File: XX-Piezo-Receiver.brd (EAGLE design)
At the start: 30.7 x 26.2 mm, 10 parts, among them IC1 TL072D, IC2 L78LXXBD/CD, J1 AVR_SPI_PROG_3X2PTH, U1 ATMEGA1284P-AU

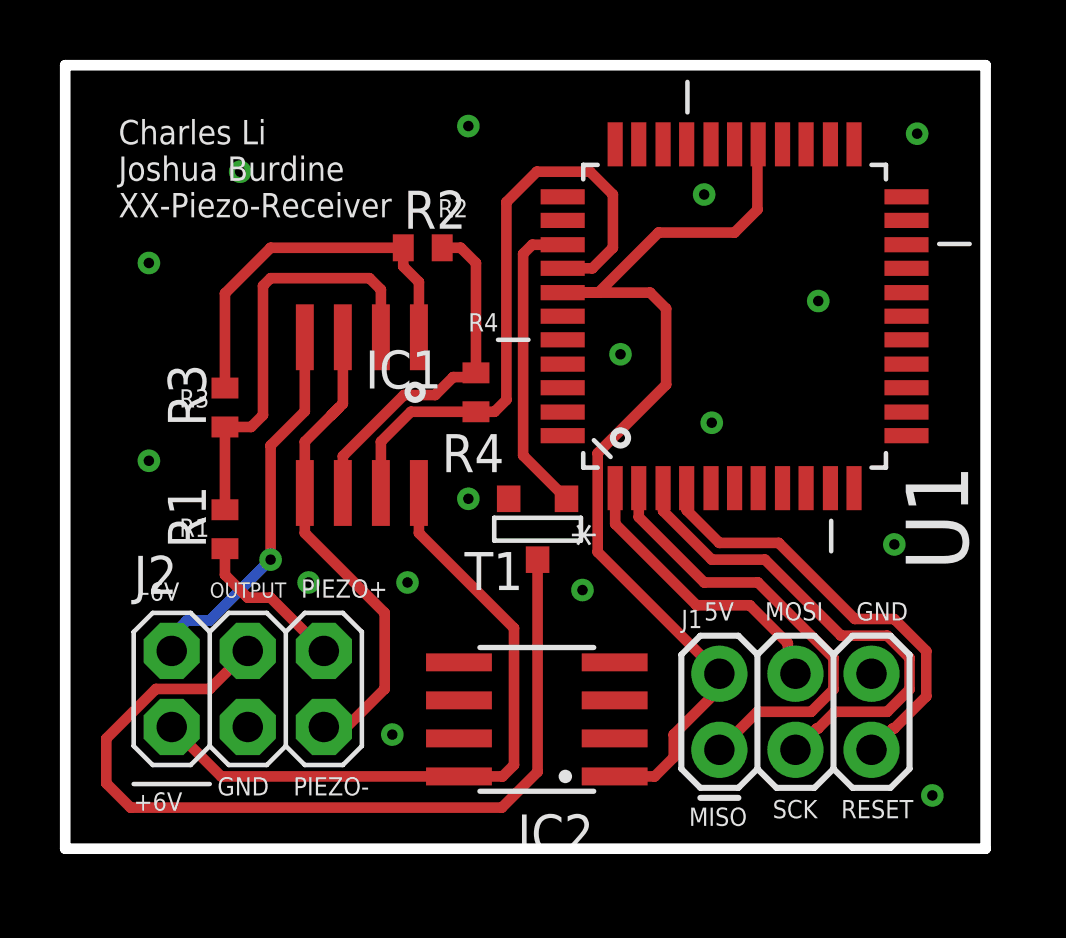
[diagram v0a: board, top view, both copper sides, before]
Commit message: Added decoupling caps and mount hole.
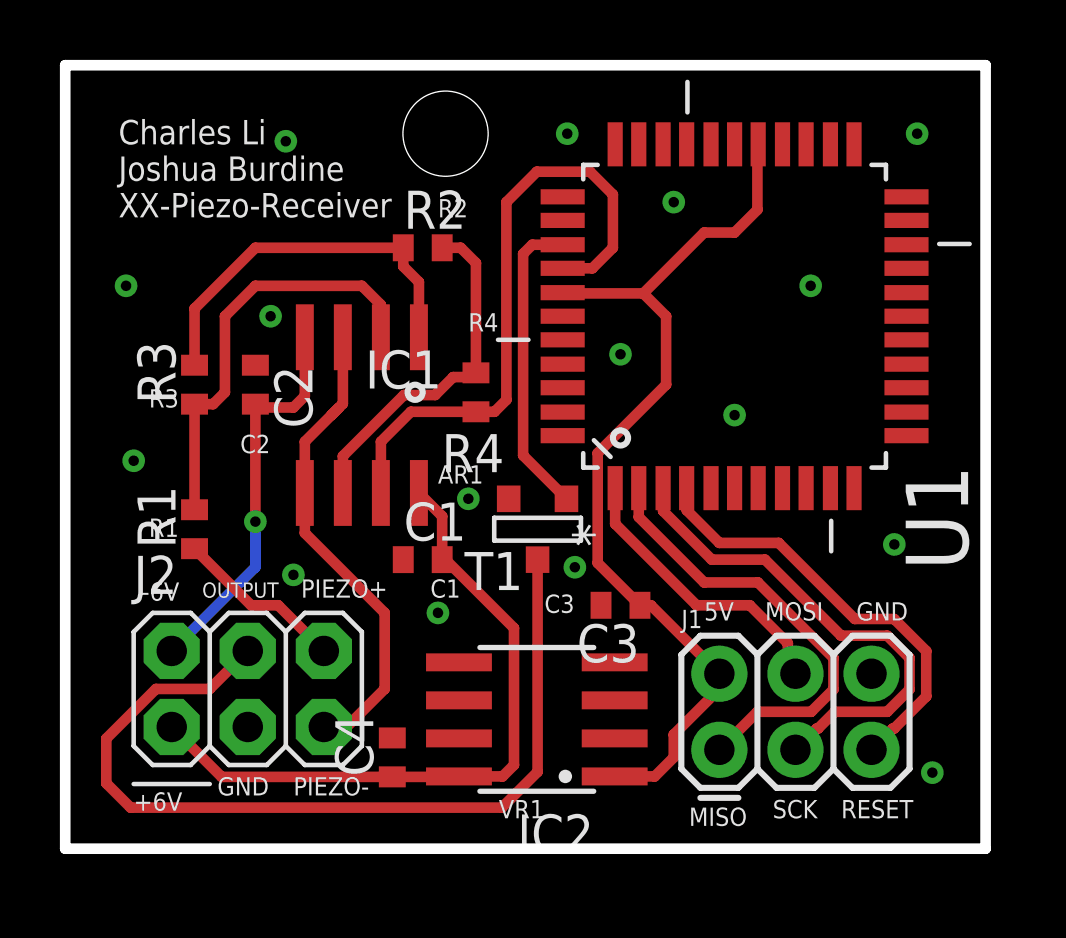
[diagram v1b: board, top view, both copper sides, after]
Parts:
- added C1, C2, C3: 0.1uF, rcl:C0402
- added C4: 0.33uF, rcl:C0402
- moved R3 1.27 mm to (4.32, 15.5)
- moved R1 1.02 mm to (4.32, 10.7)
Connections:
- net +5V: now also C3.1
- net +6V: now also C1.2, C4.1
- net -6V: now also C2.2
- net GND: now also C1.1, C2.1, C3.2, C4.2, IC2.3, IC2.6, IC2.7
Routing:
- net +5V: track 35.1 -> 31.4 mm
- net PIEZO+: track 5.23 -> 5.73 mm
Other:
- board text added: "AR1"
- board text added: "C1"
- board text added: "C2"
- board text added: "C3"
- board text added: "VR1"

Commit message: Change to 0603 components. Add new lin reg. Add new mount hole.
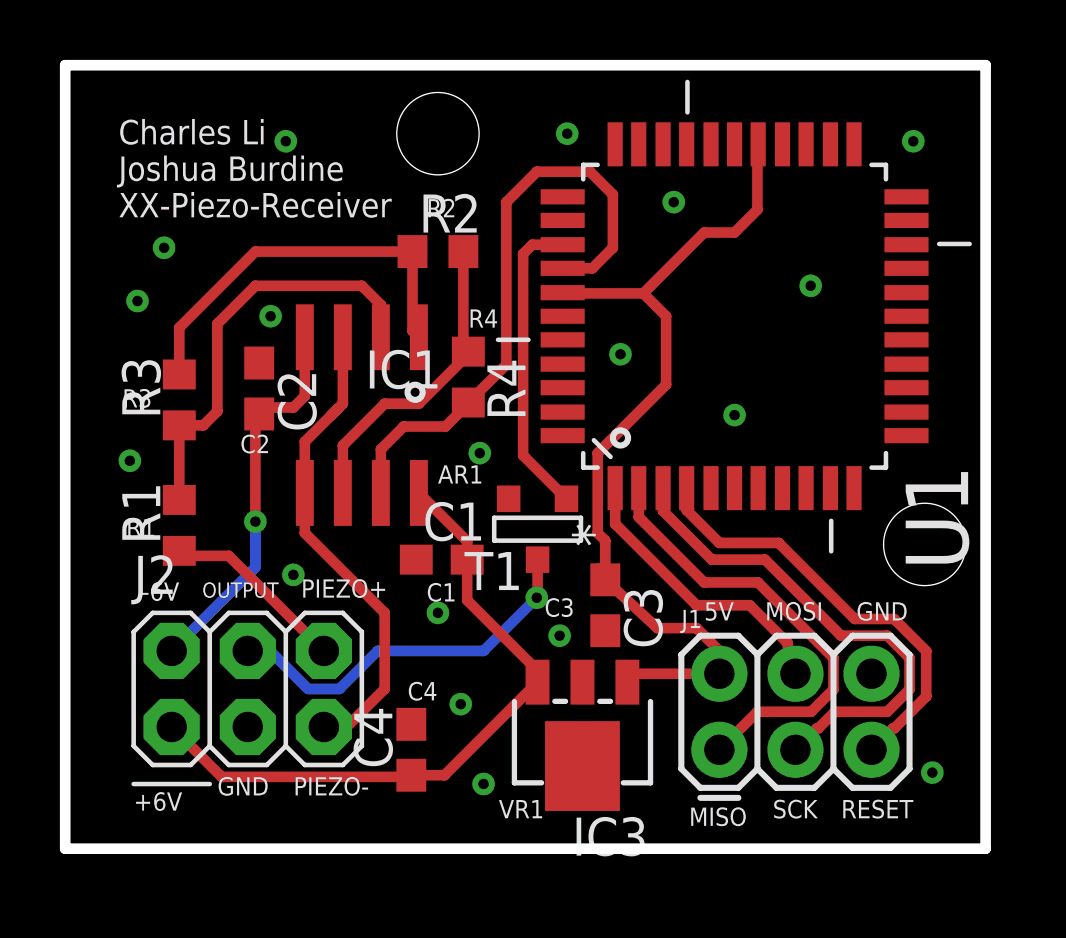
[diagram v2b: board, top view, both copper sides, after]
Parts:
- removed IC2: L78LXXBD/CD, v-reg-3:SO08
- added IC3: L78LXXCU/BU, v-reg-3:SOT89
- C1, C2, C3, C4: device rcl:C0402 -> rcl:C0603
- R1, R2, R3, R4: device rcl:R0402 -> rcl:R0603
- moved R3 0.72 mm to (3.81, 15.0)
- moved C4 0.68 mm to (11.6, 3.30)
- moved C1 0.63 mm to (12.6, 9.65)
- moved R4 0.57 mm to (13.5, 15.7)
- moved R1 0.52 mm to (3.81, 10.8)
- moved R2 0.52 mm to (12.4, 19.9)
- moved C3 0.51 mm to (18.0, 8.13), turned to 270 degrees
- moved C2 0.18 mm to (6.48, 15.4)
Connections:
- net +5V: now also IC3.1; no longer IC2.1
- net +6V: now also IC3.3; no longer IC2.8
- net GND: now also IC3.4; no longer IC2.2, IC2.3, IC2.6, IC2.7
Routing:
- net OUTPUT: track 29.7 -> 12.7 mm, vias 0 -> 1
- net +5V: track 31.4 -> 30.0 mm
- net PIEZO+2: track 11.8 -> 10.5 mm
- net OUT2: track 21.1 -> 20.3 mm
- net +6V: track 22.7 -> 22.2 mm
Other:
- board text added: "C4"

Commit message: Shifted everything 15 mil to the left.
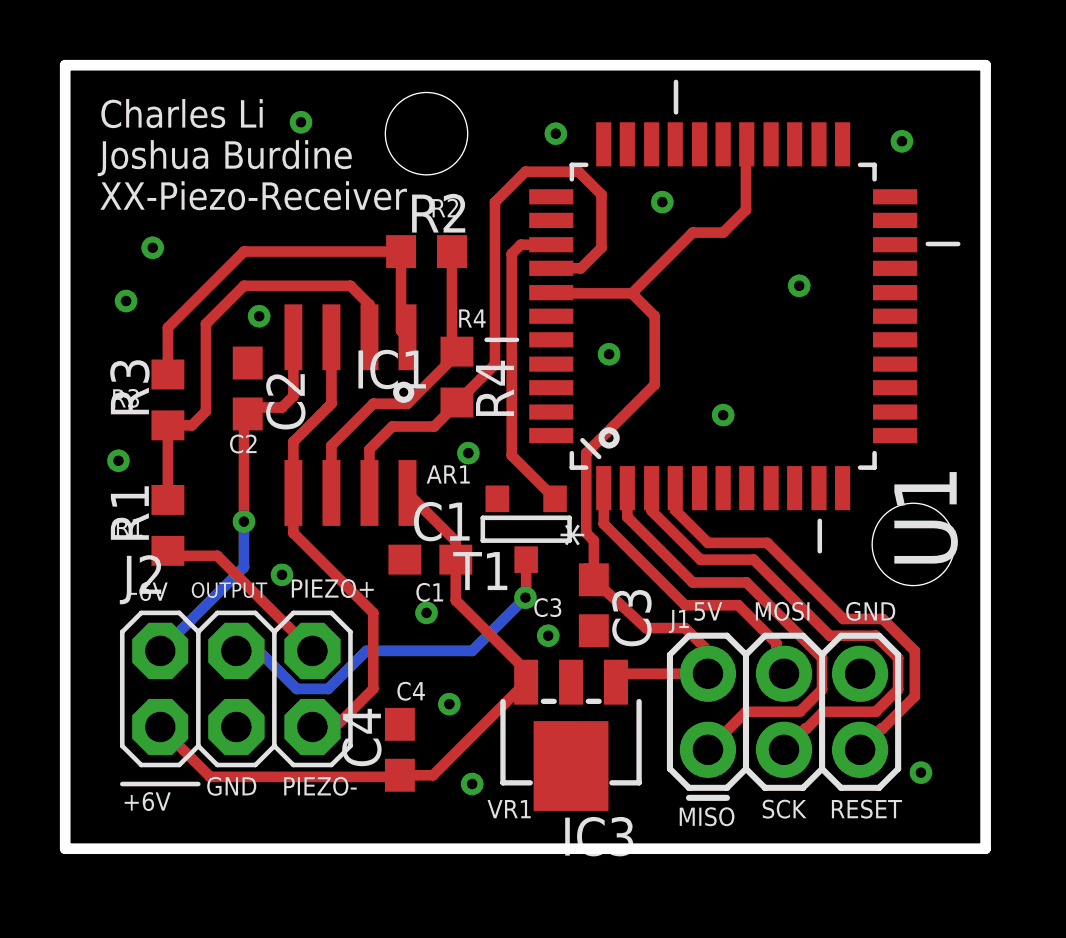
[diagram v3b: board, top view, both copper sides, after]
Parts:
- moved C1 0.38 mm to (12.2, 9.65)
- moved C2 0.38 mm to (6.10, 15.4)
- moved C3 0.38 mm to (17.7, 8.13)
- moved C4 0.38 mm to (11.2, 3.30)
- moved IC1 0.38 mm to (9.53, 14.5)
- moved IC3 0.38 mm to (16.9, 3.81)
- moved J1 0.38 mm to (21.5, 3.30)
- moved J2 0.38 mm to (5.71, 5.33)
- moved R1 0.38 mm to (3.43, 10.8)
- moved R2 0.38 mm to (12.1, 19.9)
- moved R3 0.38 mm to (3.43, 15.0)
- moved R4 0.38 mm to (13.1, 15.7)
- moved U1 0.38 mm to (22.0, 17.8)
- moved T1 0.38 mm to (15.4, 10.7)

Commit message: Moved components away from op-amp.
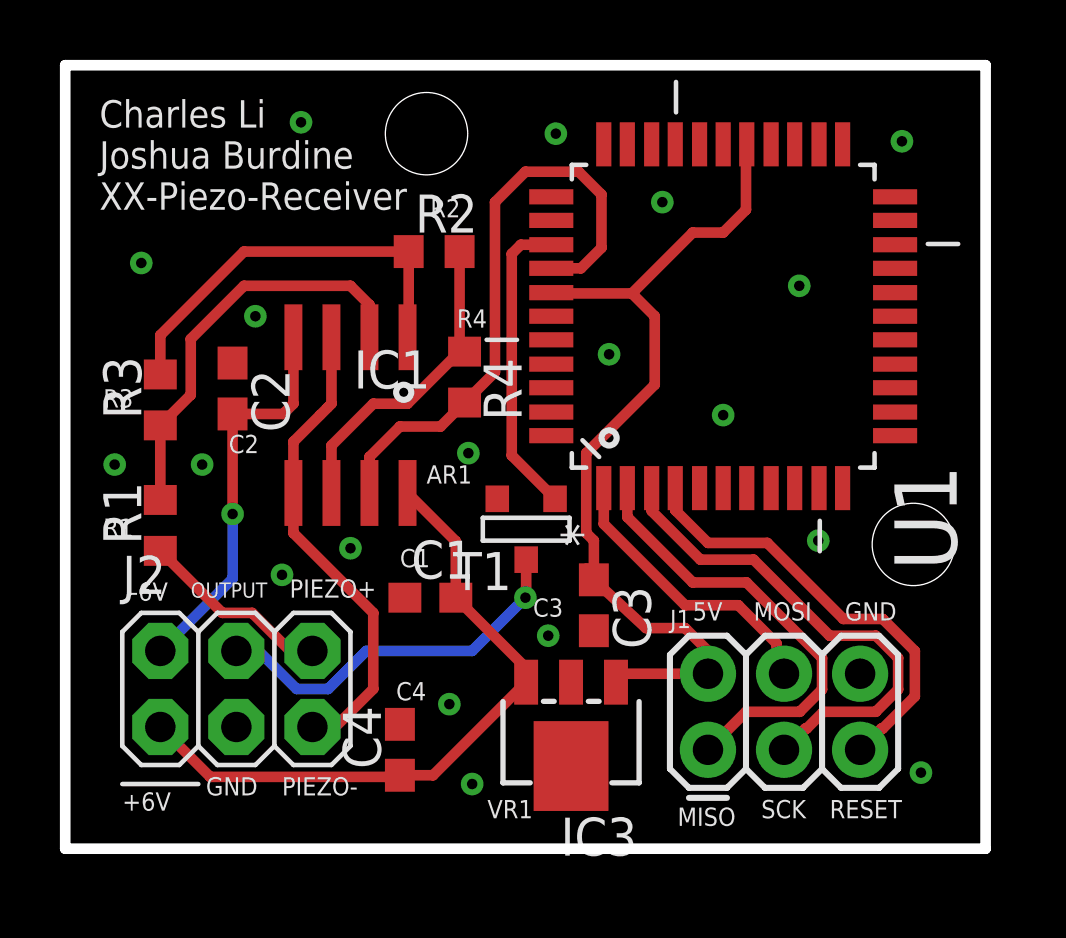
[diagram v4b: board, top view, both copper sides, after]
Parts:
- moved C1 1.27 mm to (12.2, 8.38)
- moved C2 0.51 mm to (5.59, 15.4)
- moved R2 0.25 mm to (12.3, 19.9)
- moved R4 0.25 mm to (13.3, 15.7)
- moved R1 0.25 mm to (3.17, 10.8)
- moved R3 0.25 mm to (3.17, 15.0)
